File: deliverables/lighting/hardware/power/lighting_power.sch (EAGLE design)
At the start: 9 parts, among them J1 5055780671, J2 5055780671, J3 5055780671

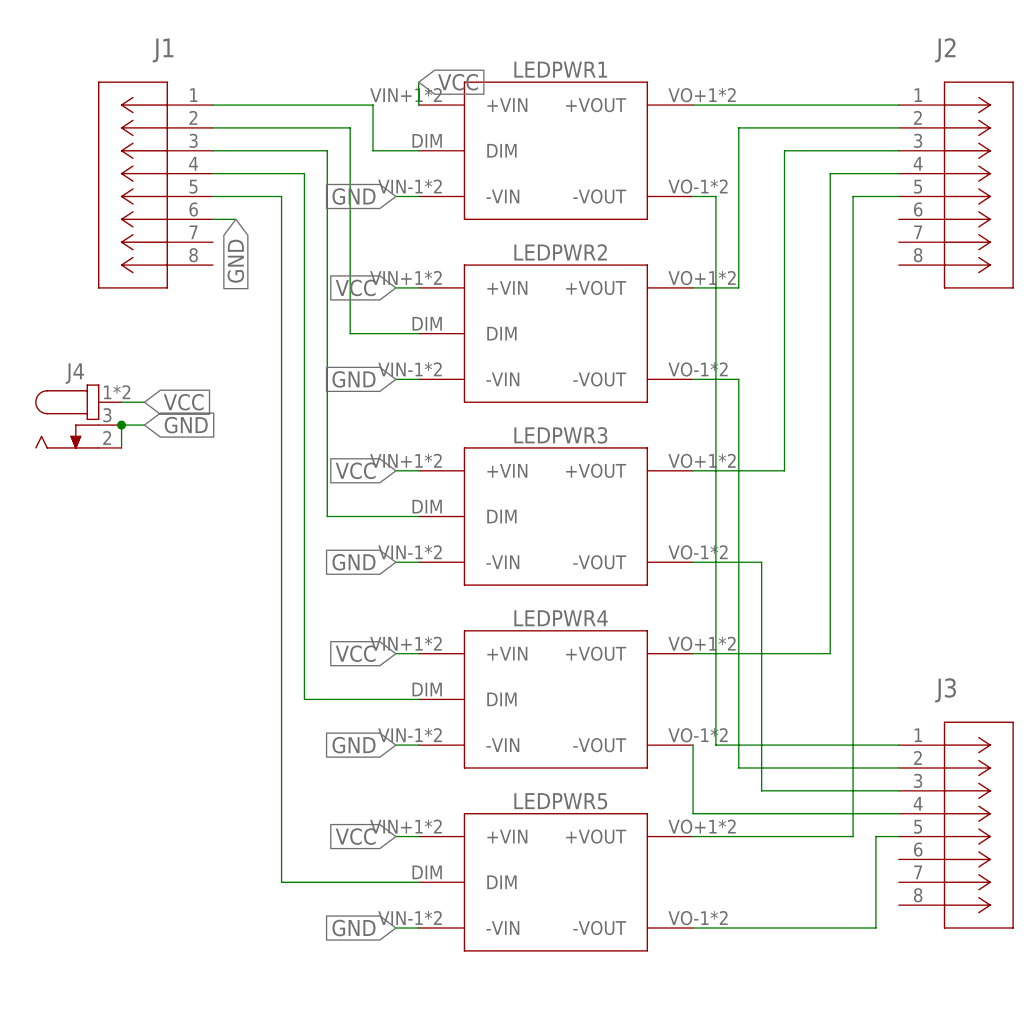
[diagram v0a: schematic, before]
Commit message: Added Supporting Files for V0.2
SCH, BRD, and PNG for both
Also FBX models
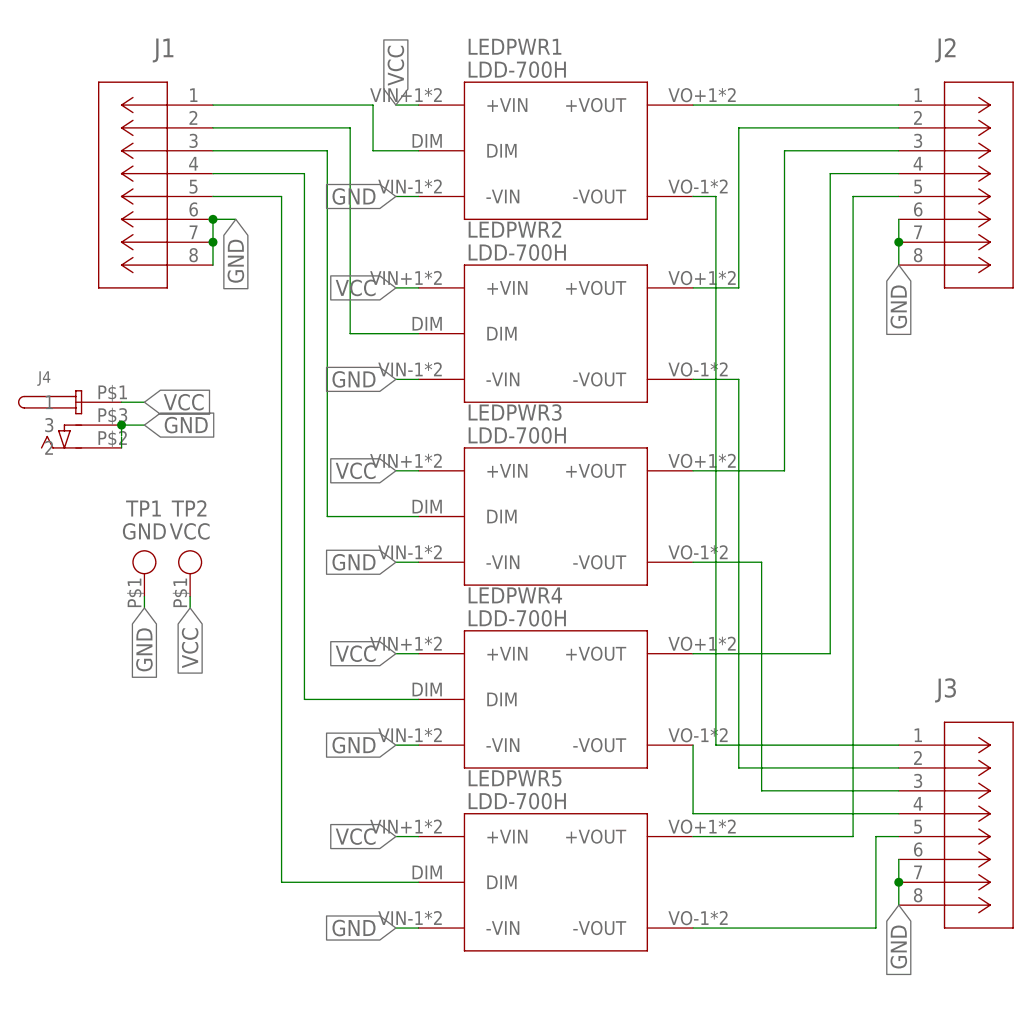
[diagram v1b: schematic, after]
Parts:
- added TP1: GND, Test Point:TP_CIRCLE_2.5MM
- added TP2: VCC, Test Point:TP_CIRCLE_2.5MM
- J1, J2, J3: value 5055780671 -> MOLEX-MICROLOCK-6PIN; device Molex Micro-Lock PLUS 6-pin (90deg):5055780671 -> Molex Micro-Lock PLUS 6-Pin 90deg:MOLEX-MICROLOCK-6PIN
- J4: value (none) -> DCBARRELJACK; device Connector:694108106102 -> DC Barrel Jack (Locking):DCBARRELJACK
- LEDPWR1, LEDPWR2, LEDPWR3, LEDPWR4, LEDPWR5: value NLDD-700H -> LDD-700H; device MeanWell NLDD-700H:NLDD-700H -> MeanWell NLDD-H Series:NLDD-300~1000H
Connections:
- new net N$16: J4.2
- net GND: now also J1.7, J1.8, J2.6, J2.7, J2.8, J3.6, J3.7, J3.8, TP1.P$1; no longer J4.2
- net VCC: now also TP2.P$1
